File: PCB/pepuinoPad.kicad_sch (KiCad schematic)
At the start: 256 parts, among them U1 Raspberry_Pi_Pico

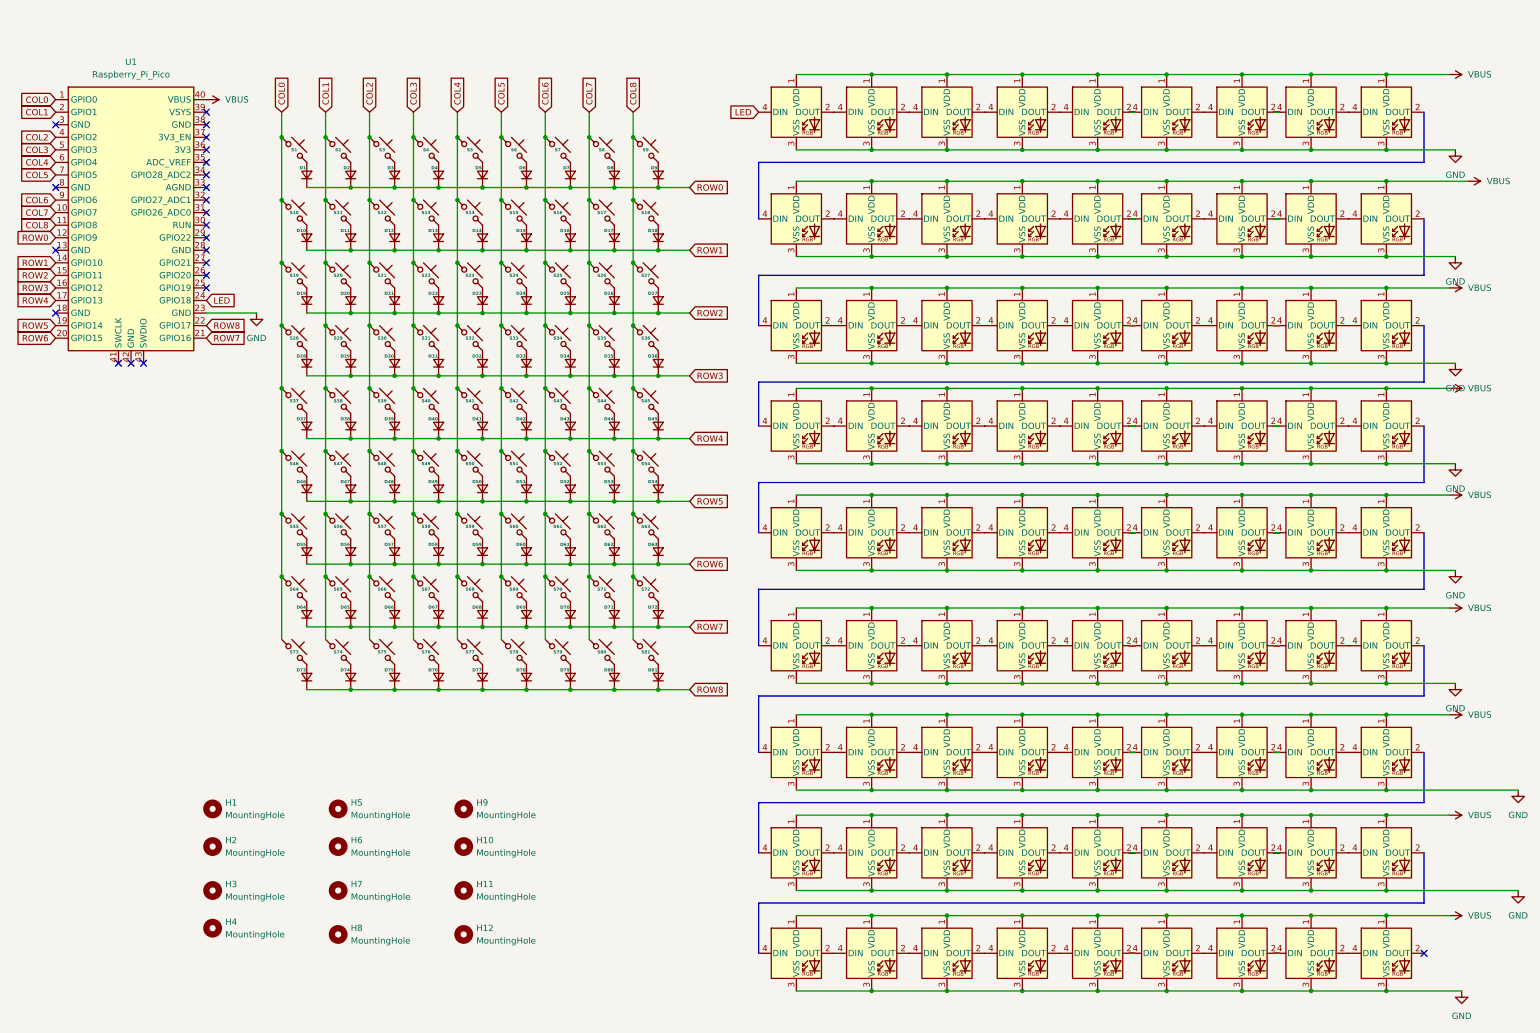
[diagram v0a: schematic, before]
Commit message: add roatry encododer + pepuino nano + update readme and img
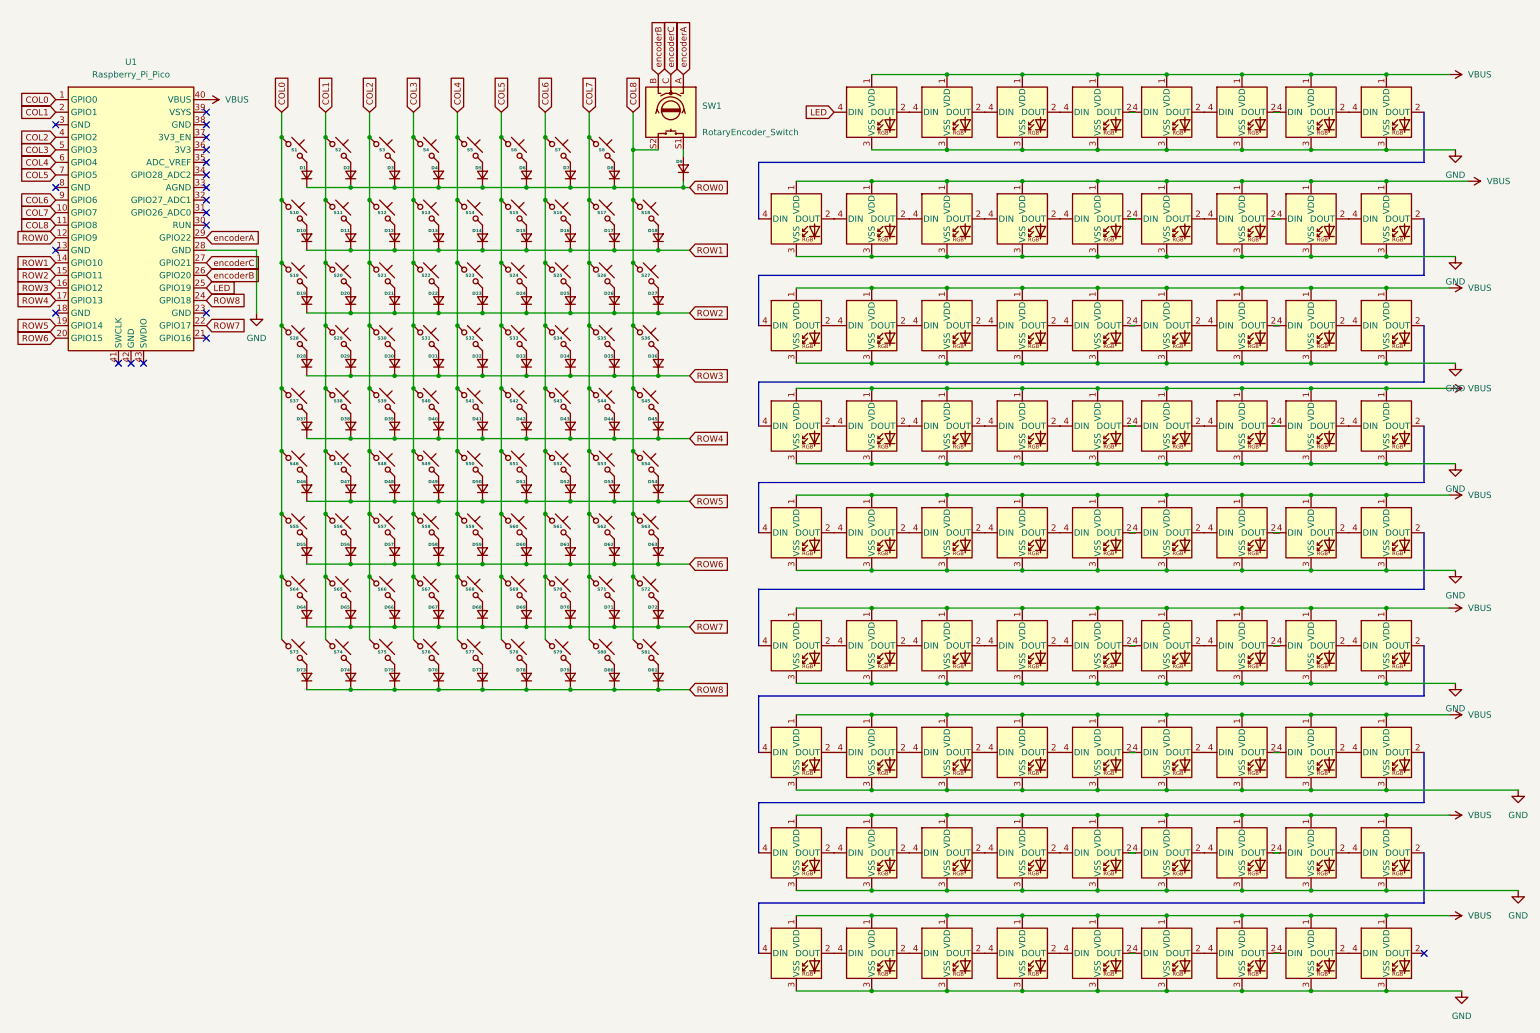
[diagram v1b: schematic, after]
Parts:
- removed D82: LED_SK6812MINI, ScottoKeebs_Components:LED_SK6812MINI, symbol ScottoKeebs:LED_SK6812MINI
- removed H1, H10, H11, H12, H2, H3, H4, H5, H6, H7, H8, H9: MountingHole, MountingHole:MountingHole_2.2mm_M2, symbol Mechanical:MountingHole
- removed S9: ~, ScottoKeebs_MX:MX_PCB_1.00u, symbol ScottoKeebs:Placeholder_Keyswitch
- added SW1: RotaryEncoder_Switch, PCM_marbastlib-various:ROT_Alps_EC11E-Switch, symbol Device:RotaryEncoder_Switch
- D100, D101, D102, D103, D104, D105, D106, D107, D108, D109, D110, D111, D112, D113, D114, D115, D116, D117, D118, D119, D120, D121, D122, D123, D124, D125, D126, D127, D128, D129, D130, D131, D132, D133, D134, D135, D136, D137, D138, D139, D140, D141, D142, D143, D144, D145, D146, D147, D148, D149, D150, D151, D152, D153, D154, D155, D156, D157, D158, D159, D160, D161, D162, D83, D84, D85, D86, D87, D88, D89, D90, D91, D92, D93, D94, D95, D96, D97, D98, D99: footprint ScottoKeebs_Components:LED_SK6812MINI -> kbd:YS-SK6812MINI-E
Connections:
- net COL8: now also SW1.S2
- net GND: now also U1.28 (GND); no longer U1.23 (GND)
- net LED: now also D83.4 (DIN), U1.25 (GPIO19); no longer U1.24 (GPIO18)
- net ROW7: now also U1.22 (GPIO17); no longer U1.21 (GPIO16)
- net ROW8: now also U1.24 (GPIO18); no longer U1.22 (GPIO17)
- net encoderB: now reaches U1.26 (GPIO20)
- net encoderB: now also SW1.B
- net encoderC: now reaches U1.27 (GPIO21)
- net encoderC: now also SW1.C
- net encoderA: now reaches U1.29 (GPIO22)
- net encoderA: now also SW1.A
- net at D9.2 (A): now also SW1.S1
- no-connect marks 23 -> 20
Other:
- moved on the sheet: D9
